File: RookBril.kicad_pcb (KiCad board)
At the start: 2 copper layers, 68.6 x 56 mm, 95 parts, among them J1 BATT_PINS, J10 TIM3_OUT_CONN, J11 Conn_01x05_Pin, J12 Conn_01x04_Pin, J13 GPIO_OUT_CONN, J2 IR_SENSOR0_PINS, J3 IR_SENSOR1_PINS, J4 IR_SENSOR2_PINS, J5 IR_SENSOR3_PINS, J6 LOW-BAT_LED_CONN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

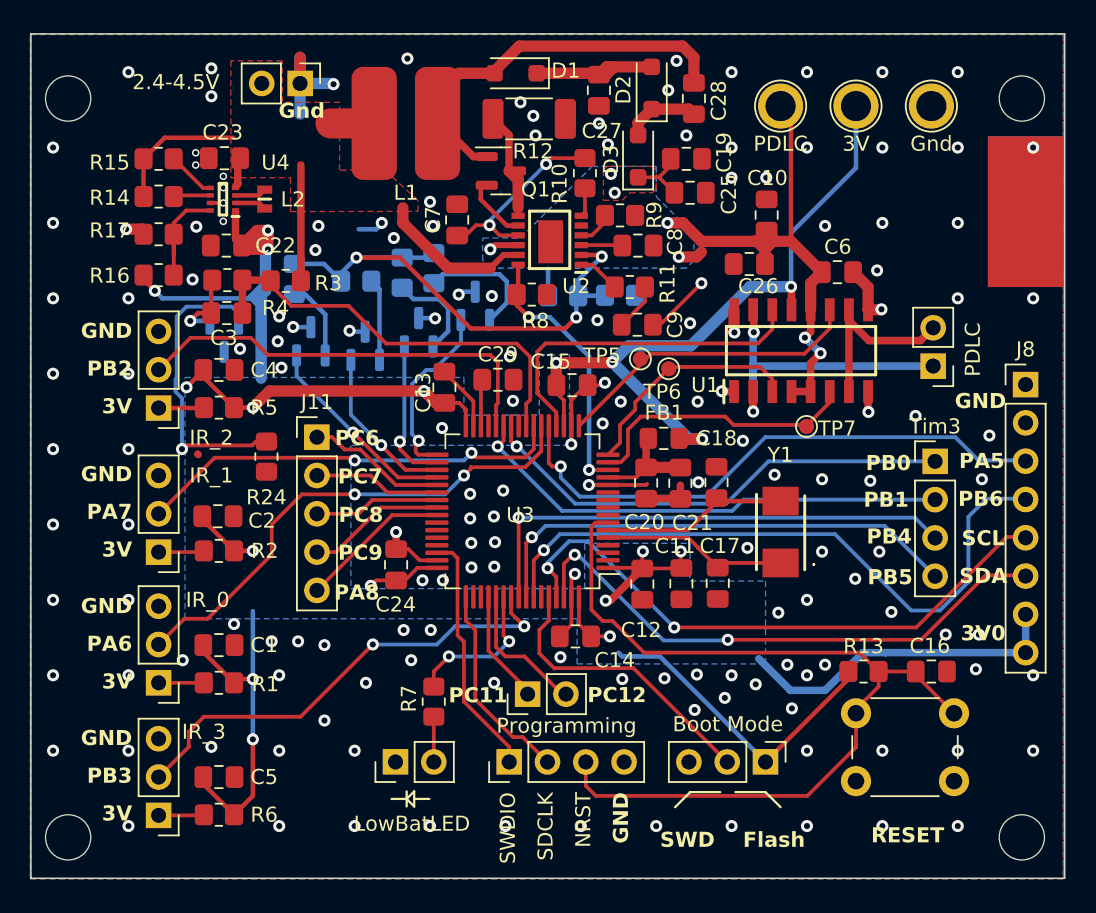
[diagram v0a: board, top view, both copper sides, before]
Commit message: VierLaagsVersie
Snel in elkaar gegooide vier laags pcb, Deze zou veel betere GND en voeding paden hebben.
Als we tijd hebben/hadden kon deze nog beter worden gemaakt door alle traces te rerouten, er zullen veel traces door minder vias kunnen nu maar dit zal werken as is.
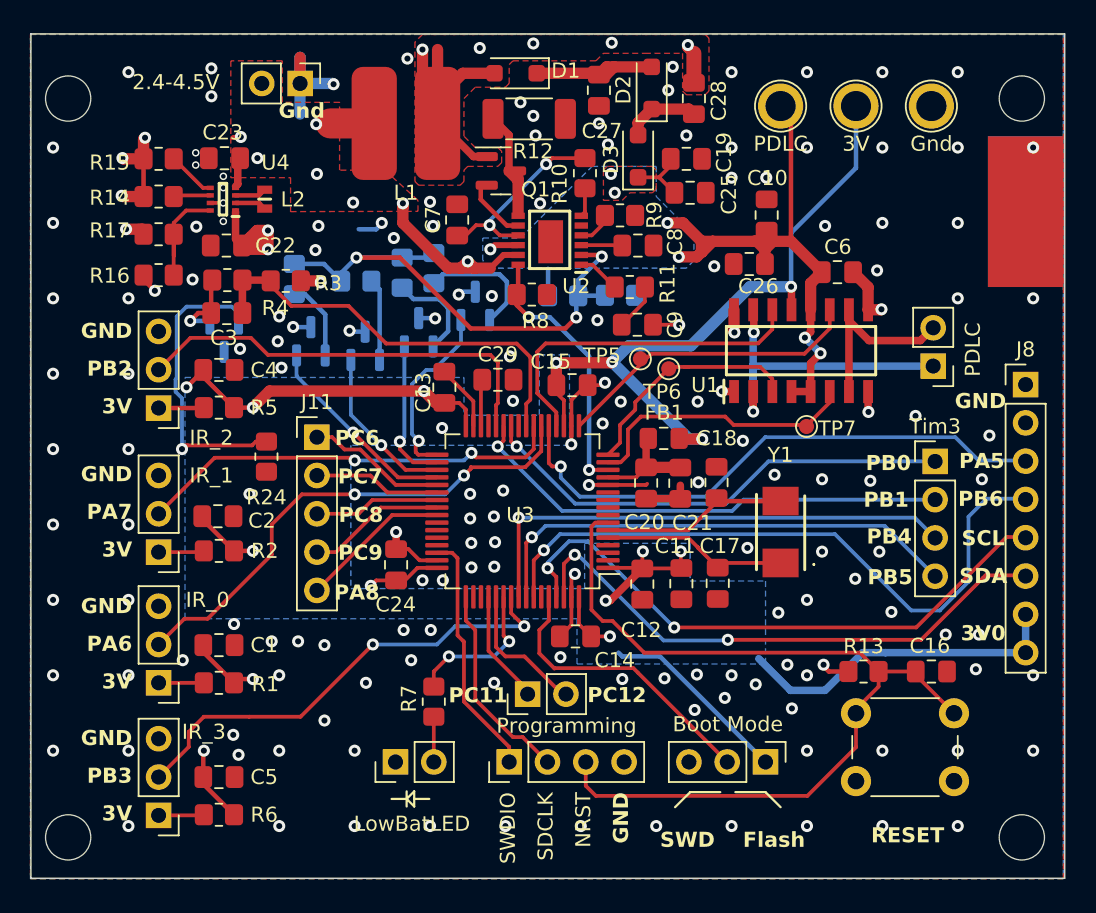
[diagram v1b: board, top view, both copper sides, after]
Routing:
- net +3V0: track 193.2 -> 164.1 mm, vias 18 -> 19
- net +BATT: track 32.1 -> 26.6 mm, vias 0 -> 11
- net GND: track 56.2 -> 53.5 mm, vias 159 -> 157
- net VCC: track 43.2 -> 45.0 mm
- net Net-(D1-A): track 25.9 -> 24.8 mm, vias 0 -> 5
- net (no net): vias 0 -> 4
- added copper zone on In2.Cu, net +3V0
- added copper zone on In2.Cu, net +BATT
- added copper zone on In1.Cu, net GND
- added copper zone on F.Cu, net Net-(D1-A)
- added copper zone on In2.Cu, net Net-(D1-A)
- added copper zone on In2.Cu, net VCC
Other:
- copper layers 2 -> 4

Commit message: PCB4Lv0.1
(vergat goed te saven)
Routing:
- net GND: vias 157 -> 160
- net (no net): vias 4 -> 0
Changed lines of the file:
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@@
     (effects (font (size 1 1) (thickness 0.15) bold) (justify right bottom))
   )
-  (via (at 137.3 115.275) (size 0.8) (drill 0.4) (layers "F.Cu" "B.Cu") (net 0))
-  (via (at 168.85 82.875) (size 0.8) (drill 0.4) (layers "F.Cu" "B.Cu") (net 0))
-  (via (at 157.3 78.7) (size 0.8) (drill 0.4) (layers "F.Cu" "B.Cu") (net 0))
-  (via (at 138.025 97.975) (size 0.8) (drill 0.4) (layers "F.Cu" "B.Cu") (net 0))
   (segment (start 137 92.25) (end 138.25 92.25) (width 0.3) (layer "F.Cu") (net 1))
   (segment (start 134.9625 117.2125) (end 137 119.25) (width 0.3) (layer "F.Cu") (net 1))
@@
   (via (at 150.85 103.7) (size 0.8) (drill 0.4) (layers "F.Cu" "B.Cu") (free) (net 2))
   (via (at 178.2 103.6) (size 0.8) (drill 0.4) (layers "F.Cu" "B.Cu") (free) (net 2))
-  (via (at 136.95 113.95) (size 0.8) (drill 0.4) (layers "F.Cu" "B.Cu") (free) (net 2))
+  (via (at 137 115) (size 0.8) (drill 0.4) (layers "F.Cu" "B.Cu") (free) (net 2))
   (via (at 175 70) (size 0.8) (drill 0.4) (layers "F.Cu" "B.Cu") (free) (net 2))
   (via (at 174 112.2) (size 0.8) (drill 0.4) (layers "F.Cu" "B.Cu") (free) (net 2))
@@
   (via (at 150.8 93.6) (size 0.8) (drill 0.4) (layers "F.Cu" "B.Cu") (free) (net 2))
   (via (at 134.4612 75.3484) (size 0.5) (drill 0.3) (layers "F.Cu" "B.Cu") (free) (net 2))
+  (via (at 138 97.75) (size 0.8) (drill 0.4) (layers "F.Cu" "B.Cu") (free) (net 2))
+  (via (at 168.75 83) (size 0.8) (drill 0.4) (layers "F.Cu" "B.Cu") (free) (net 2))
   (via (at 175 75) (size 0.8) (drill 0.4) (layers "F.Cu" "B.Cu") (free) (net 2))
   (via (at 186.6 97) (size 0.8) (drill 0.4) (layers "F.Cu" "B.Cu") (free) (net 2))
@@
   (via (at 141.25 107.75) (size 0.8) (drill 0.4) (layers "F.Cu" "B.Cu") (free) (net 2))
   (via (at 167.55 112.3) (size 0.8) (drill 0.4) (layers "F.Cu" "B.Cu") (free) (net 2))
+  (via (at 157.75 77.75) (size 0.8) (drill 0.4) (layers "F.Cu" "B.Cu") (free) (net 2))
   (via (at 185 120) (size 0.8) (drill 0.4) (layers "F.Cu" "B.Cu") (free) (net 2))
   (via (at 139.5 107.75) (size 0.8) (drill 0.4) (layers "F.Cu" "B.Cu") (free) (net 2))

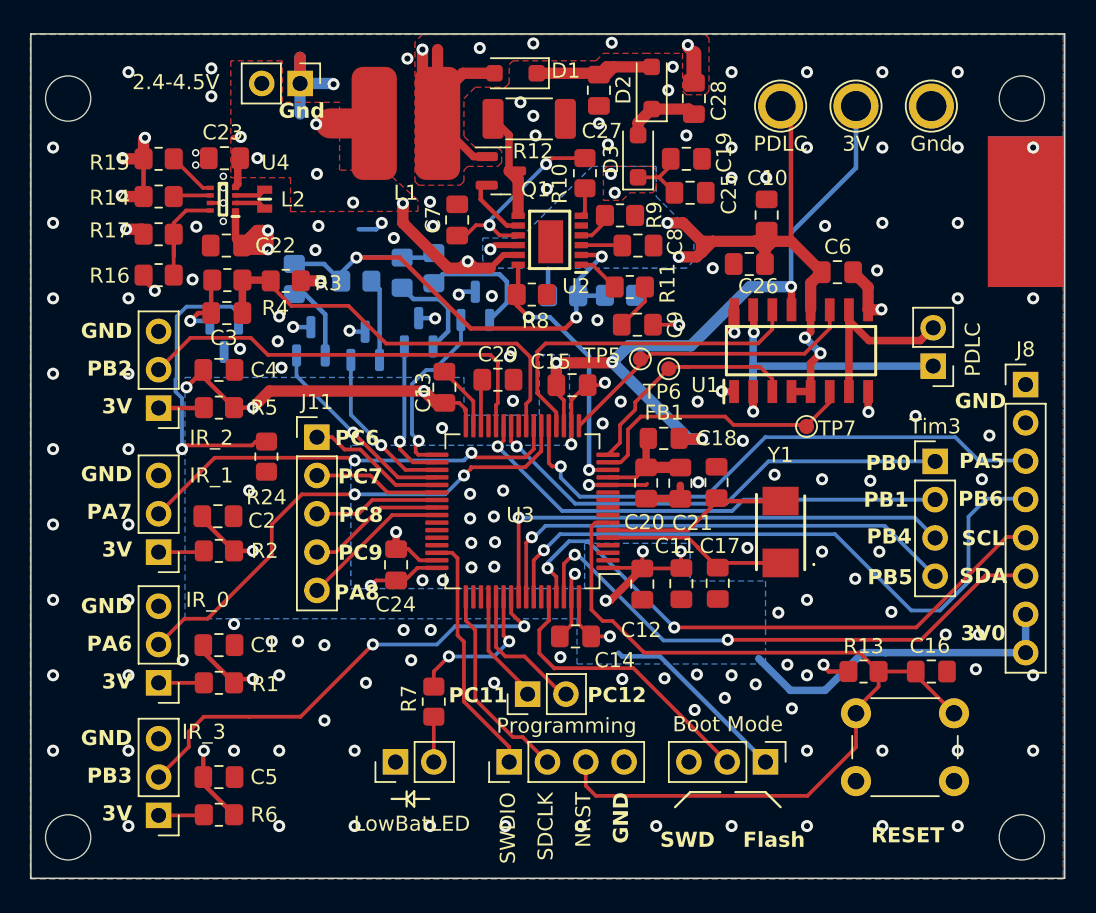
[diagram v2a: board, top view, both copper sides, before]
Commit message: PCB4Lv0.2
Paar dingen nog extra vergeten, IR LED toegevoegd aan de bottom side.
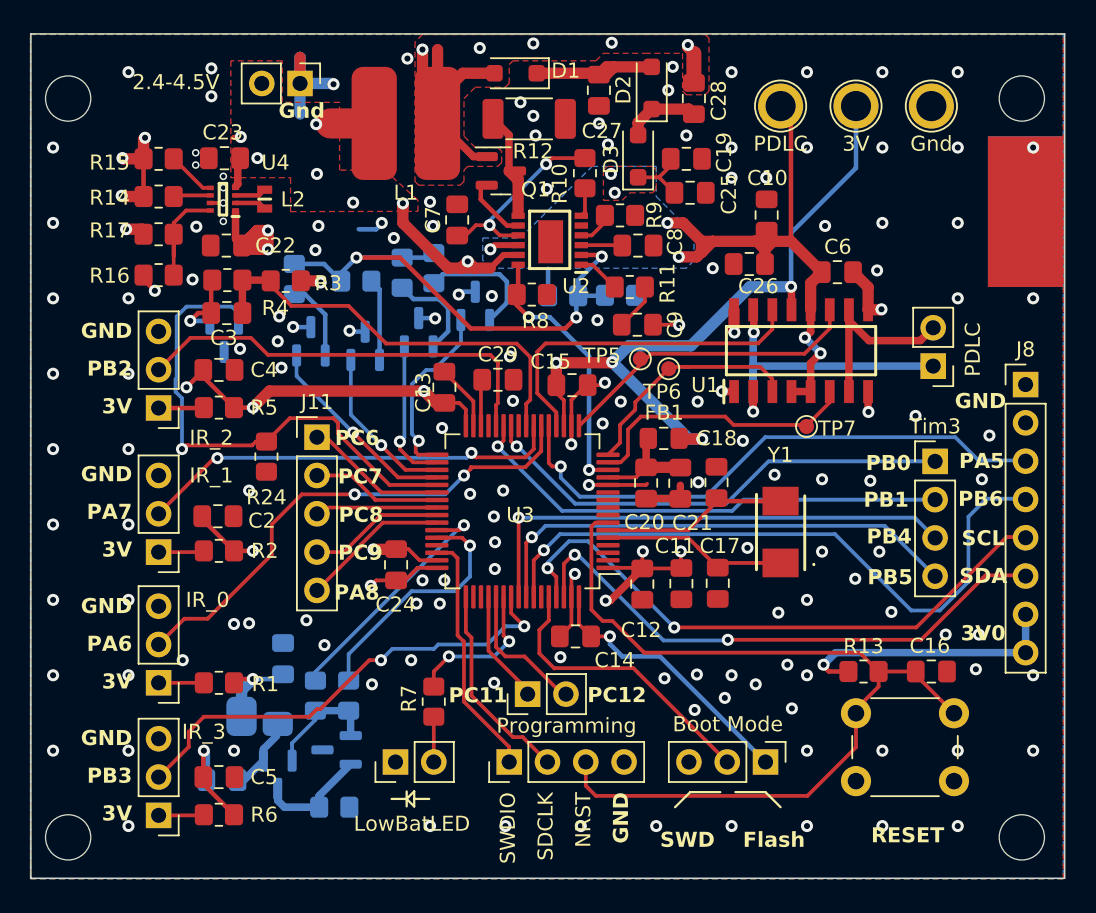
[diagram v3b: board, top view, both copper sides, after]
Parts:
- added C30: 100n, Capacitor_SMD:C_0805_2012Metric_Pad1.18x1.45mm_HandSolder, B.Cu at (136.2, 117.0)
- added D4: LED, Components:IRLED, B.Cu at (139.9, 114.0)
- added Q7: NPN, Package_TO_SOT_SMD:SOT-23, B.Cu at (139.9, 116.6)
- added Q8: NPN, Package_TO_SOT_SMD:SOT-23, B.Cu at (143.8, 115.0)
- added R25: 6, Resistor_SMD:R_0805_2012Metric_Pad1.20x1.40mm_HandSolder, B.Cu at (143.7, 118.8)
- added R26: 450, Resistor_SMD:R_0805_2012Metric_Pad1.20x1.40mm_HandSolder, B.Cu at (144.6, 111.3)
- added R27: 670, Resistor_SMD:R_0805_2012Metric_Pad1.20x1.40mm_HandSolder, B.Cu at (142.4, 111.3)
- C1: moved to B.Cu
- moved C1 4.34 mm to (140.2, 108.9), turned to 90 degrees
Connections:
- J11 pad 1: /MCU/PC6 -> /MCU/PC7
- J11 pad 2: /MCU/PC7 -> /MCU/PC8
- J11 pad 3: /MCU/PC8 -> /MCU/PC9
- J11 pad 4: /MCU/PC9 -> /MCU/PA8
- J11 pad 5: /MCU/PA8 -> /MCU/PA9
- U3 pad 37: /MCU/PC6 -> /VBAT_Gate
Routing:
- net /MCU/PA10: track 0.00 -> 16.6 mm, vias 0 -> 1
- net /MCU/PA11: track 0.00 -> 16.4 mm, vias 0 -> 1
- net /VBAT_Gate: track 20.6 -> 34.8 mm
- net /MCU/PA9: track 0.00 -> 9.88 mm
- net /MCU/PC6: track 9.26 -> 0.00 mm
- net Net-(Q7-B): track 0.00 -> 7.86 mm
- net Net-(Q7-E): track 0.00 -> 7.41 mm
- net Net-(D4-K): track 0.00 -> 5.08 mm
- net /MCU/PA8: track 10.0 -> 8.97 mm
- net /MCU/PC7: track 8.42 -> 9.47 mm
- net /MCU/PC9: track 9.18 -> 8.12 mm
- net +3V0: track 164.1 -> 163.2 mm
- net GND: track 53.5 -> 54.0 mm, vias 160 -> 150
- removed copper zone on B.Cu, net +3V0

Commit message: Ordered this one
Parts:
- removed TP5, TP6, TP7: TestPoint, TestPoint:TestPoint_Pad_D1.0mm
- added INA1: TestPoint, TestPoint:TestPoint_Pad_D1.0mm, F.Cu at (166.0, 89.8)
- added INB1: TestPoint, TestPoint:TestPoint_Pad_D1.0mm, F.Cu at (175.0, 93.5)
- added PWM1: TestPoint, TestPoint:TestPoint_Pad_D1.0mm, F.Cu at (164.0, 89.0)
- C1: moved to F.Cu
- J8: value Conn_01x08_Pin -> Conn_01x09_Pin; footprint Connector_PinHeader_2.54mm:PinHeader_1x08_P2.54mm_Vertical -> Connector_PinHeader_2.54mm:PinHeader_1x09_P2.54mm_Vertical
- moved R16 5.01 mm to (136.5, 81.2), turned to 180 degrees
- moved C1 4.34 mm to (136.0, 108.0), turned to 180 degrees
- moved C22 3.77 mm to (140.2, 81.2), turned to 0 degrees
- moved Q5 2.26 mm to (152.8, 87.8)
- moved R23 1.77 mm to (152.0, 83.2)
- moved R18 1.63 mm to (159.2, 83.2), turned to 90 degrees
- moved R19 1.59 mm to (162.2, 83.2), turned to 90 degrees
- moved R21 0.62 mm to (145.0, 83.2), turned to 90 degrees
- moved R20 0.53 mm to (141.2, 83.2)
- moved Q4 0.50 mm to (149.2, 87.8)
- moved R17 0.50 mm to (132.0, 81.2)
- moved Q3 0.40 mm to (145.8, 87.8)
- moved R22 0.35 mm to (148.5, 83.3)
- moved C2 0.21 mm to (136.0, 99.2), turned to 180 degrees
- moved C11 0.19 mm to (166.5, 104.0)
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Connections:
- J8 pad 5: /MCU/PB8 -> /MCU/PB7
- J8 pad 6: /MCU/PB9 -> /MCU/PB8
- J8 pad 7: +3V0 -> /MCU/PB9
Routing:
- net +3V0: track 163.2 -> 91.9 mm, vias 19 -> 14
- net /MCU/PB7: track 0.00 -> 38.3 mm, vias 0 -> 1
- net Net-(U2-FBX): track 35.6 -> 24.0 mm, vias 3 -> 1
- net /VBAT_Gate: track 34.8 -> 27.0 mm
- net /MCU/PB8: track 39.7 -> 36.1 mm
- net Net-(Q5-D): track 8.32 -> 5.14 mm
- net Net-(U4-FB): track 7.68 -> 4.61 mm
- net Net-(J7-Pin_1): track 23.1 -> 20.2 mm
- net /PDLC-BOOST_VOUT-FBbit3: track 12.4 -> 9.50 mm
- net Net-(Q6-D): track 5.19 -> 8.02 mm
- net /MCU/PB9: track 37.2 -> 34.5 mm
- net GND: track 54.0 -> 51.8 mm
- net /MCU/PB6: track 43.5 -> 41.5 mm
- net VCC: track 45.0 -> 43.2 mm
- net Net-(Q4-D): track 6.56 -> 5.11 mm
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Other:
- board text added: "Designed by Mathijs, Wouter, Ediz, Gino and Kevin"
- board text added: "Interactive Glasses Prototype 2"
- board text added: "November 2023"
- board text added: "PB7"
